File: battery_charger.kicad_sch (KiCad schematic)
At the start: 0 parts

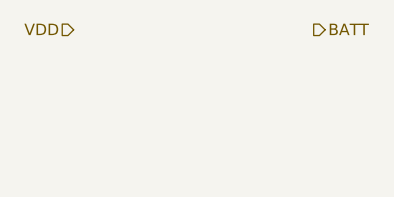
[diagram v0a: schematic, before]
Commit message: Added discharge Mosfet.
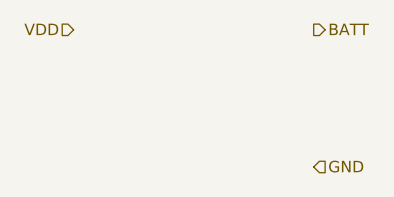
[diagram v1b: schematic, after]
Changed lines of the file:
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@@
 	(generator_version "8.0")
 	(paper "A4")
+	(hierarchical_label "GND"
+		(shape input)
+		(at 49.53 40.64 0)
+		(fields_autoplaced yes)
+		(effects
+			(font
+				(size 1.27 1.27)
+			)
+			(justify left)
+		)
+	)
 	(hierarchical_label "VDD"
 		(shape input)

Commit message: Prepared STS1_BATT_TEST.
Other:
- note added: "Choose a battery charger here. The charger should be enable via the ENABLE signal. It shall be dormant, if the ENABLE signal is low. There are two options here. 1.) (simple) Just place a pin strip here. The battery charger will then be connected via jumper vias to this pin strip 2.) (complex) Choose a battery charger IC and place it here."
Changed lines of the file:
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@@
 	(generator_version "8.0")
 	(paper "A4")
+	(text "Choose a battery charger here. The charger should be enable via the \nENABLE signal. It shall be dormant, if the ENABLE signal is low. \nThere are two options here. \n1.) (simple) Just place a pin strip here. The battery charger will then\nbe connected via jumper vias to this pin strip \n2.) (complex) Choose a battery charger IC and place it here."
+		(exclude_from_sim no)
+		(at 24.892 42.164 0)
+		(effects
+			(font
+				(size 1.27 1.27)
+			)
+			(justify left)
+		)
+	)
 	(hierarchical_label "GND"
 		(shape input)
-		(at 49.53 40.64 0)
+		(at 49.53 58.42 0)
 		(fields_autoplaced yes)
 		(effects
@@
 		)
 	)
+	(hierarchical_label "ENABLE"
+		(shape input)
+		(at 22.86 58.42 180)
+		(fields_autoplaced yes)
+		(effects
+			(font
+				(size 1.27 1.27)
+			)
+			(justify right)
+		)
+	)
